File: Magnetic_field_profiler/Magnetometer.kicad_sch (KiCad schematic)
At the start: 3 parts, among them U2 MLX90393

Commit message: Symbol Properties Edits
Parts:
- renumbered C9 to C32, C10 to C33, U2 to U9
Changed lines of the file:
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@@
 		(on_board yes)
 		(dnp no)
-		(property "Reference" "U2"
+		(property "Reference" "U9"
 			(at 150.114 78.74 0)
 			(effects
@@
 		(property "Description" "Wide dynamic range magnetometer"
 			(at 139.7 76.962 0)
+			(effects
+				(font
+					(size 1.27 1.27)
+				)
+				(hide yes)
+			)
+		)
+		(property "Manufacturer" ""
+			(at 139.7 92.71 0)
+			(effects
+				(font
+					(size 1.27 1.27)
+				)
+				(hide yes)
+			)
+		)
+		(property "Manufacturer Part Number" ""
+			(at 139.7 92.71 0)
 			(effects
 				(font
@@
 		(dnp no)
 		(fields_autoplaced yes)
-		(property "Reference" "#PWR040"
+		(property "Reference" "#PWR039"
 			(at 138.43 116.84 0)
 			(effects
@@
 		(dnp no)
 		(fields_autoplaced yes)
-		(property "Reference" "C10"
+		(property "Reference" "C33"
 			(at 132.08 68.5799 0)
 			(effects
@@
 		)
 		(property "Description" "Unpolarized capacitor"
+			(at 128.27 69.85 0)
+			(effects
+				(font
+					(size 1.27 1.27)
+				)
+				(hide yes)
+			)
+		)
+		(property "Manufacturer" ""
+			(at 128.27 69.85 0)
+			(effects
+				(font
+					(size 1.27 1.27)
+				)
+				(hide yes)
+			)
+		)
+		(property "Manufacturer Part Number" ""
 			(at 128.27 69.85 0)
 			(effects
@@
 		(dnp no)
 		(fields_autoplaced yes)
-		(property "Reference" "#PWR06"
+		(property "Reference" "#PWR035"
 			(at 138.43 67.31 0)
 			(effects
@@
 		(dnp no)
 		(fields_autoplaced yes)
-		(property "Reference" "#PWR011"
+		(property "Reference" "#PWR038"
 			(at 157.48 93.98 0)
 			(effects
@@
 		(dnp no)
 		(fields_autoplaced yes)
-		(property "Reference" "C9"
+		(property "Reference" "C32"
 			(at 120.65 68.5799 0)
 			(effects
@@
 		)
 		(property "Description" "Unpolarized capacitor"
+			(at 116.84 69.85 0)
+			(effects
+				(font
+					(size 1.27 1.27)
+				)
+				(hide yes)
+			)
+		)
+		(property "Manufacturer" ""
+			(at 116.84 69.85 0)
+			(effects
+				(font
+					(size 1.27 1.27)
+				)
+				(hide yes)
+			)
+		)
+		(property "Manufacturer Part Number" ""
 			(at 116.84 69.85 0)
 			(effects
@@
 		(dnp no)
 		(fields_autoplaced yes)
-		(property "Reference" "#PWR07"
+		(property "Reference" "#PWR036"
 			(at 116.84 82.55 0)
 			(effects

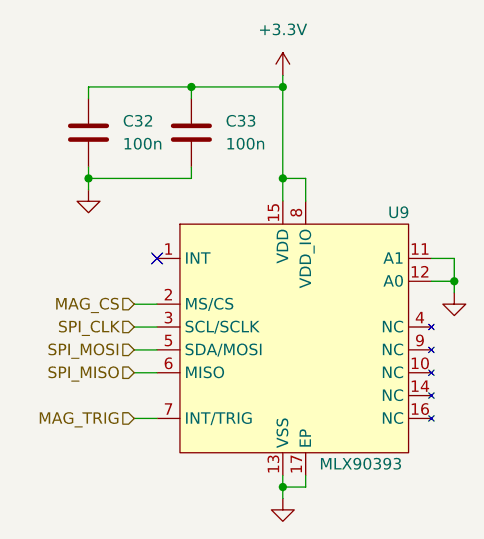
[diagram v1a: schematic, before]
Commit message: IO expander wchematic and footprint updated. Adjusted the schematic representation of the magnetometer array.
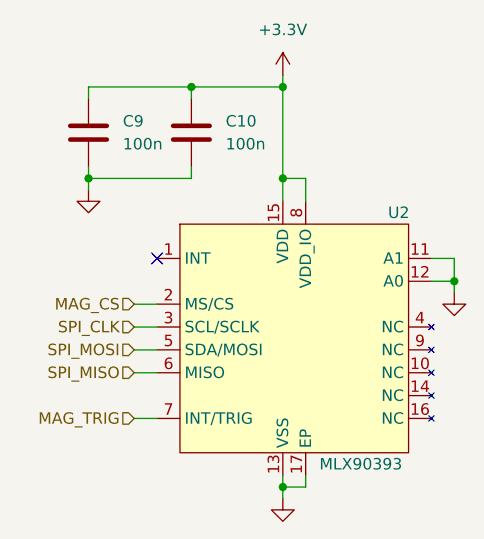
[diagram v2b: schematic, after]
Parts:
- renumbered C33 to C10, C32 to C9, U9 to U2

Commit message: IO expander connections complete and PCB layout restarted
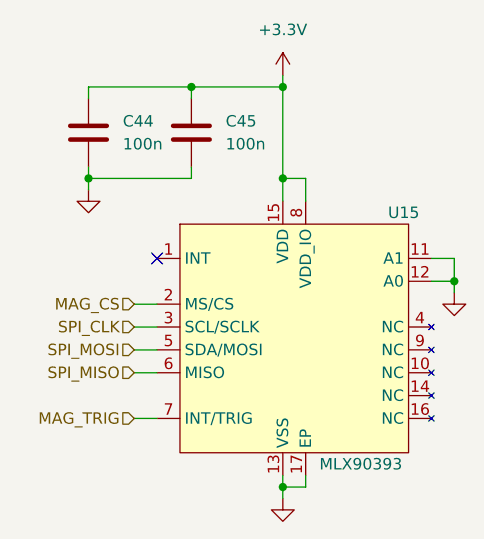
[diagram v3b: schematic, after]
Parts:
- renumbered C9 to C44, C10 to C45, U2 to U15

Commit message: BOM Information Update
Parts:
- U15: Distributor Link (none) -> https://www.digikey.com/en/products/detail/melexis-technolo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; Manufacturer (none) -> Melexis Technologies NV; Manufacturer Part Number (none) -> MLX90393SLW-ABA-011-RE
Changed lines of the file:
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@@
 			)
 		)
-		(property "Manufacturer" ""
+		(property "Manufacturer" "Melexis Technologies NV"
 			(at 139.7 92.71 0)
 			(effects
@@
 			)
 		)
-		(property "Manufacturer Part Number" ""
+		(property "Manufacturer Part Number" "MLX90393SLW-ABA-011-RE "
+			(at 139.7 92.71 0)
+			(effects
+				(font
+					(size 1.27 1.27)
+				)
+				(hide yes)
+			)
+		)
+		(property "Distributor Link" "https://www.digikey.com/en/products/detail/melexis-technologies-nv/MLX90393SLW-ABA-011-RE/5031683"
 			(at 139.7 92.71 0)
 			(effects
@@
 			)
 		)
+		(property "Distributor Link" ""
+			(at 128.27 69.85 0)
+			(effects
+				(font
+					(size 1.27 1.27)
+				)
+				(hide yes)
+			)
+		)
 		(pin "2"
 		)
@@
 			(at 116.84 69.85 0)
 			(effects
+				(font
+					(size 1.27 1.27)
+				)
+				(hide yes)
+			)
+		)
+		(property "Distributor Link" ""
+			(at 116.84 69.85 0)
+			(effects

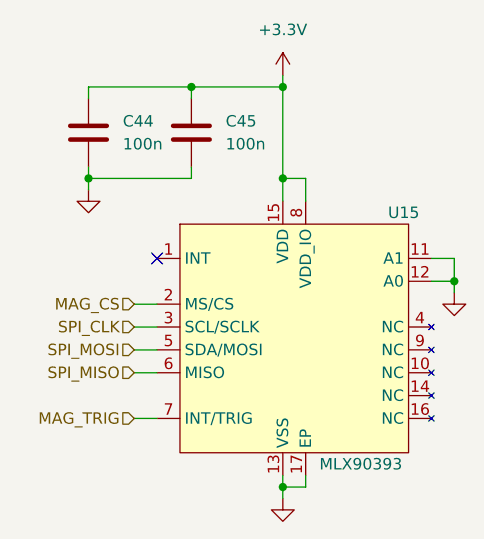
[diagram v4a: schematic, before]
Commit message: DC-DC converter rework
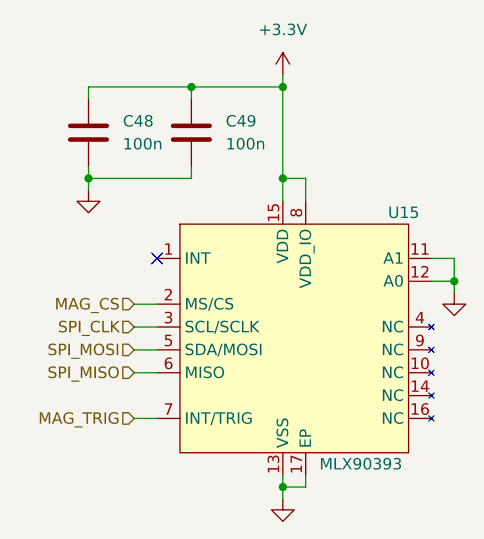
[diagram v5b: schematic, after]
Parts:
- renumbered C44 to C48, C45 to C49

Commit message: Continued adding component description and sourcing information
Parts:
- C48, C49: footprint Capacitor_SMD:C_0402_1005Metric -> Capacitor_SMD:C_0201_0603Metric; Distributor Link (none) -> https://www.digikey.com/en/products/detail/murata-electroni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; Manufacturer (none) -> Murata Electronics; Manufacturer Part Number (none) -> GRM033C81E104KE14D
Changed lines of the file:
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@@
 			)
 		)
-		(property "Footprint" "Capacitor_SMD:C_0402_1005Metric"
+		(property "Footprint" "Capacitor_SMD:C_0201_0603Metric"
 			(at 129.2352 73.66 0)
 			(effects
@@
 			)
 		)
-		(property "Manufacturer" ""
+		(property "Manufacturer" "Murata Electronics"
 			(at 128.27 69.85 0)
 			(effects
@@
 			)
 		)
-		(property "Manufacturer Part Number" ""
+		(property "Manufacturer Part Number" "GRM033C81E104KE14D"
 			(at 128.27 69.85 0)
 			(effects
@@
 			)
 		)
-		(property "Distributor Link" ""
+		(property "Distributor Link" "https://www.digikey.com/en/products/detail/murata-electronics/GRM033C81E104KE14D/5027488"
 			(at 128.27 69.85 0)
 			(effects
@@
 			)
 		)
-		(property "Footprint" "Capacitor_SMD:C_0402_1005Metric"
+		(property "Footprint" "Capacitor_SMD:C_0201_0603Metric"
 			(at 117.8052 73.66 0)
 			(effects
@@
 			)
 		)
-		(property "Manufacturer" ""
+		(property "Manufacturer" "Murata Electronics"
 			(at 116.84 69.85 0)
 			(effects
@@
 			)
 		)
-		(property "Manufacturer Part Number" ""
+		(property "Manufacturer Part Number" "GRM033C81E104KE14D"
 			(at 116.84 69.85 0)
 			(effects
@@
 			)
 		)
-		(property "Distributor Link" ""
+		(property "Distributor Link" "https://www.digikey.com/en/products/detail/murata-electronics/GRM033C81E104KE14D/5027488"
 			(at 116.84 69.85 0)
 			(effects
